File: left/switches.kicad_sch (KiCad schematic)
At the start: 38 parts, among them K11 KEYSW_RGB, K12 KEYSW_RGB, K13 KEYSW_RGB, K14 KEYSW_RGB, K15 KEYSW_RGB, K16 KEYSW_RGB, K21 KEYSW_RGB, K22 KEYSW_RGB, K23 KEYSW_RGB, K24 KEYSW_RGB, K25 KEYSW_RGB, K26 KEYSW_RGB, K31 KEYSW_RGB, K32 KEYSW_RGB, K33 KEYSW_RGB, K34 KEYSW_RGB, K35 KEYSW_RGB, K36 KEYSW_RGB, K41 KEYSW_RGB, K42 KEYSW_RGB, K43 KEYSW_RGB, K44 KEYSW_RGB, K45 KEYSW_RGB, K46 KEYSW_RGB, K51 KEYSW_RGB, K52 KEYSW_RGB, K53 KEYSW_RGB, K54 KEYSW_RGB, K55 KEYSW_RGB, K56 KEYSW_RGB, K61 KEYSW_RGB, K62 KEYSW_RGB, K63 KEYSW_RGB, K64 KEYSW_RGB, K65 KEYSW_RGB, K66 KEYSW_RGB, SW2 Rotary_Encoder_Switch

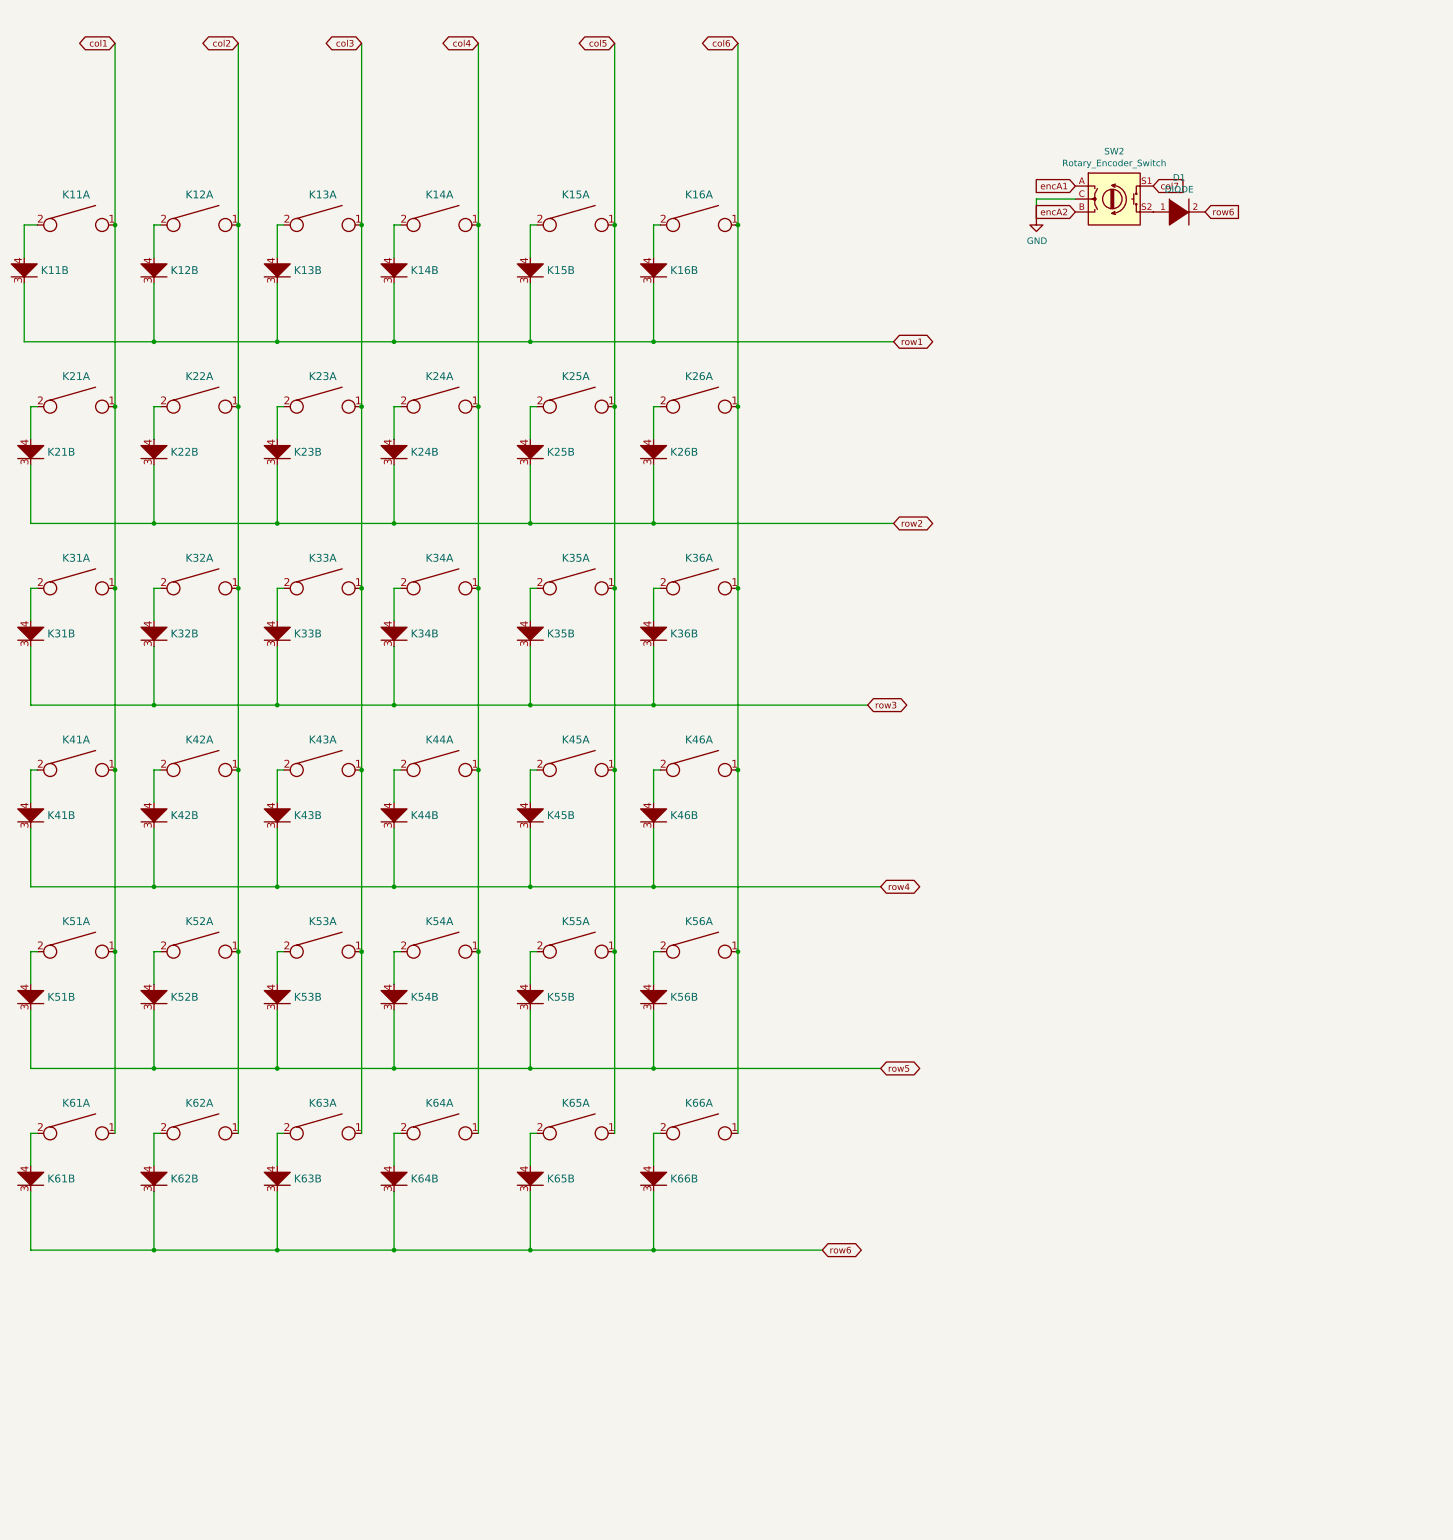
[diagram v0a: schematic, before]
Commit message: Broke out keys into individual components so that the BOM and pick and place are easier to generate.
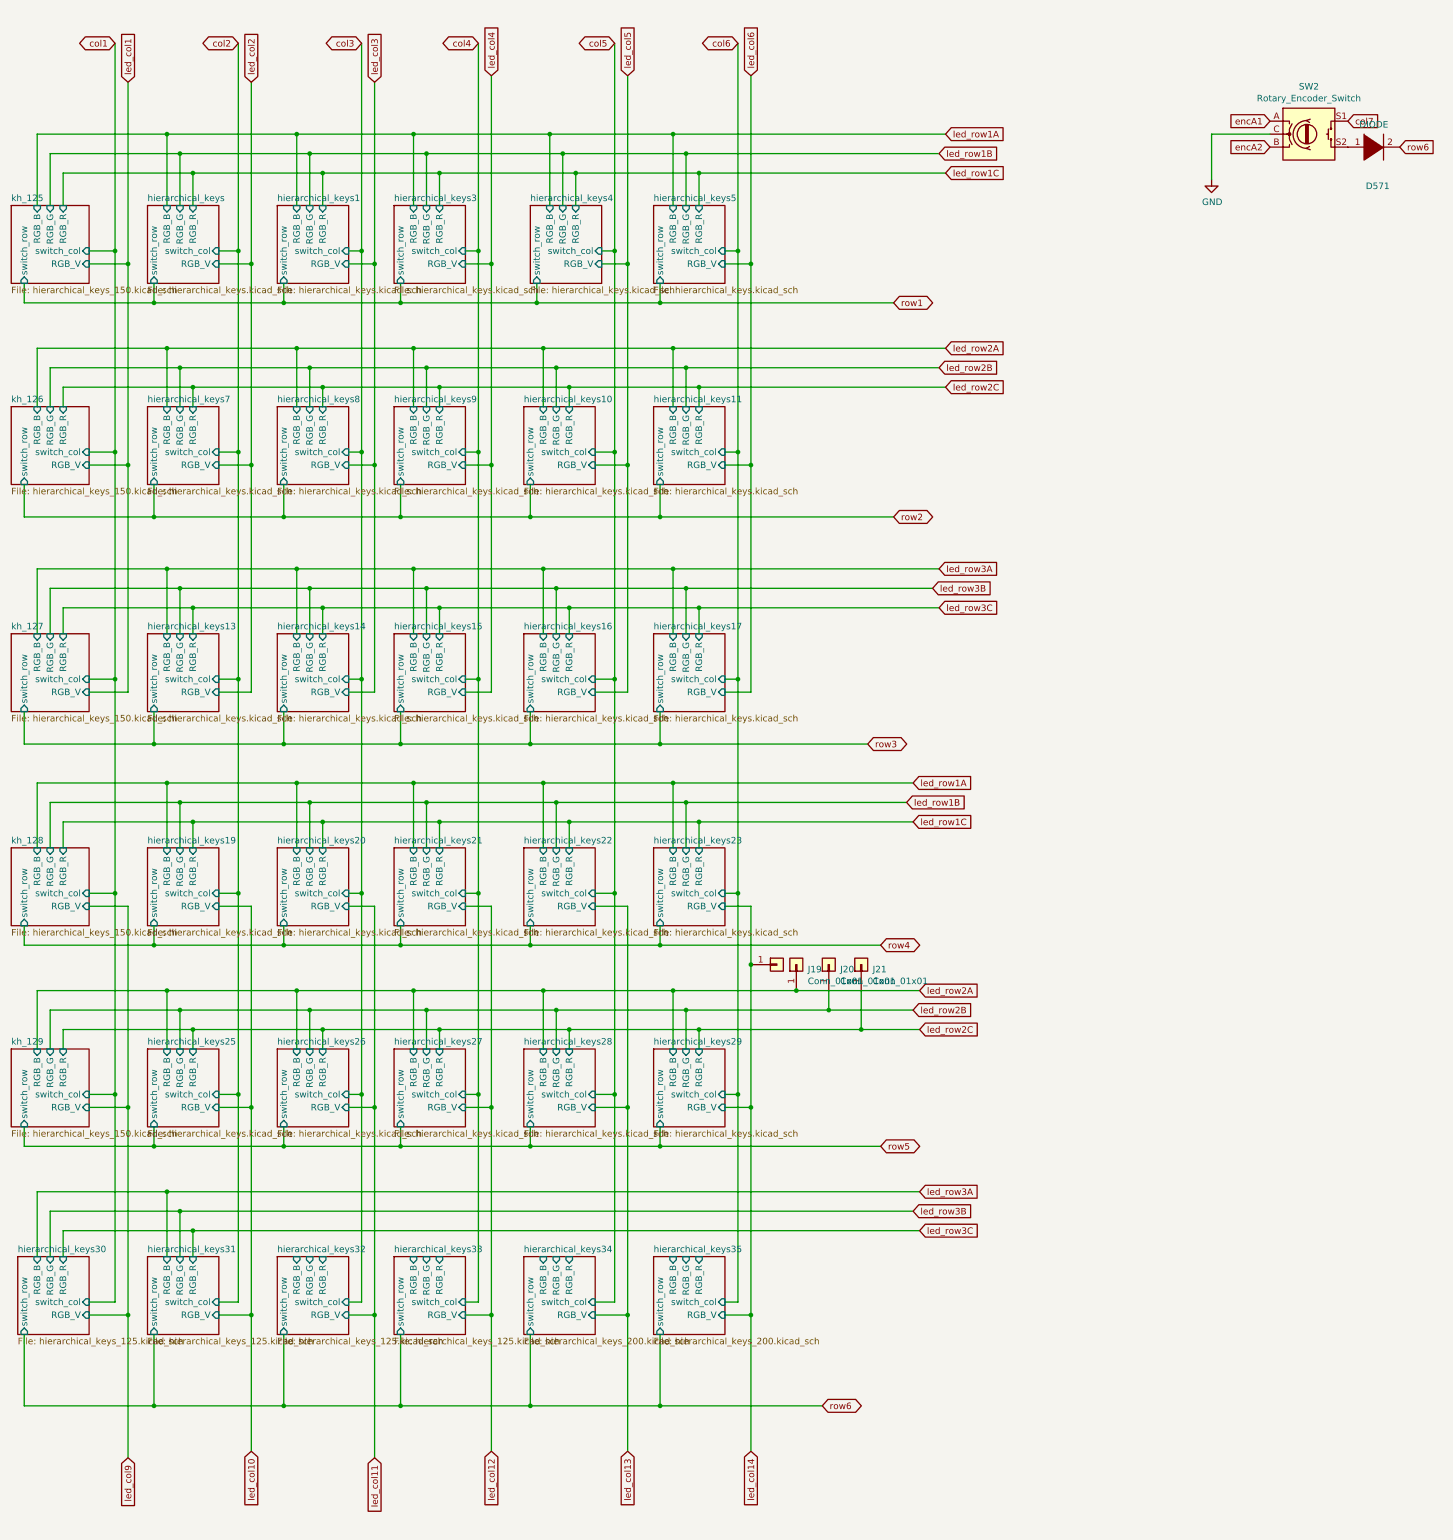
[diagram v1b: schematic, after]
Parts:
- removed K11, K21, K31, K41, K51: KEYSW_RGB, vladkvit_keyb:Hybrid_PCB_150H_hotswap_diode_RGB_rot, symbol vladkvit_keyb:KEYSW_RGB
- removed K12, K13, K14, K15, K16, K22, K23, K24, K25, K26, K32, K33, K34, K35, K36, K42, K43, K44, K45, K46, K52, K53, K54, K55, K56: KEYSW_RGB, vladkvit_keyb:Hybrid_PCB_100H_hotswap_diode_RGB_rot, symbol vladkvit_keyb:KEYSW_RGB
- removed K61, K62, K63, K64: KEYSW_RGB, vladkvit_keyb:Hybrid_PCB_125H_hotswap_diode_RGB_rot, symbol vladkvit_keyb:KEYSW_RGB
- removed K65, K66: KEYSW_RGB, vladkvit_keyb:Hybrid_PCB_200H_hotswap_diode_RGB, symbol vladkvit_keyb:KEYSW_RGB
- added J18, J19, J20, J21: Conn_01x01, TestPoint:TestPoint_Pad_D1.5mm, symbol Connector_Generic:Conn_01x01
- D571: renamed from D1; footprint Diode_SMD:D_0805_2012Metric_Pad1.15x1.40mm_HandSolder -> Diode_SMD:D_SOD-123
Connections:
- new net led_col14: J18.1 (Pin_1)
- new net led_row2A: J19.1 (Pin_1)
- new net led_row2B: J20.1 (Pin_1)
- new net led_row2C: J21.1 (Pin_1)
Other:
- added sheet hierarchical_keys (hierarchical_keys.kicad_sch)
- added sheet hierarchical_keys1 (hierarchical_keys.kicad_sch)
- added sheet hierarchical_keys10 (hierarchical_keys.kicad_sch)
- added sheet hierarchical_keys11 (hierarchical_keys.kicad_sch)
- added sheet hierarchical_keys13 (hierarchical_keys.kicad_sch)
- added sheet hierarchical_keys14 (hierarchical_keys.kicad_sch)
- added sheet hierarchical_keys15 (hierarchical_keys.kicad_sch)
- added sheet hierarchical_keys16 (hierarchical_keys.kicad_sch)
- added sheet hierarchical_keys17 (hierarchical_keys.kicad_sch)
- added sheet hierarchical_keys19 (hierarchical_keys.kicad_sch)
- added sheet hierarchical_keys20 (hierarchical_keys.kicad_sch)
- added sheet hierarchical_keys21 (hierarchical_keys.kicad_sch)
- added sheet hierarchical_keys22 (hierarchical_keys.kicad_sch)
- added sheet hierarchical_keys23 (hierarchical_keys.kicad_sch)
- added sheet hierarchical_keys25 (hierarchical_keys.kicad_sch)
- added sheet hierarchical_keys26 (hierarchical_keys.kicad_sch)
- added sheet hierarchical_keys27 (hierarchical_keys.kicad_sch)
- added sheet hierarchical_keys28 (hierarchical_keys.kicad_sch)
- added sheet hierarchical_keys29 (hierarchical_keys.kicad_sch)
- added sheet hierarchical_keys3 (hierarchical_keys.kicad_sch)
- added sheet hierarchical_keys30 (hierarchical_keys_125.kicad_sch)
- added sheet hierarchical_keys31 (hierarchical_keys_125.kicad_sch)
- added sheet hierarchical_keys32 (hierarchical_keys_125.kicad_sch)
- added sheet hierarchical_keys33 (hierarchical_keys_125.kicad_sch)
- added sheet hierarchical_keys34 (hierarchical_keys_200.kicad_sch)
- added sheet hierarchical_keys35 (hierarchical_keys_200.kicad_sch)
- added sheet hierarchical_keys4 (hierarchical_keys.kicad_sch)
- added sheet hierarchical_keys5 (hierarchical_keys.kicad_sch)
- added sheet hierarchical_keys7 (hierarchical_keys.kicad_sch)
- added sheet hierarchical_keys8 (hierarchical_keys.kicad_sch)
- added sheet hierarchical_keys9 (hierarchical_keys.kicad_sch)
- added sheet kh_125 (hierarchical_keys_150.kicad_sch)
- added sheet kh_126 (hierarchical_keys_150.kicad_sch)
- added sheet kh_127 (hierarchical_keys_150.kicad_sch)
- added sheet kh_128 (hierarchical_keys_150.kicad_sch)
- added sheet kh_129 (hierarchical_keys_150.kicad_sch)
- moved on the sheet: D571, SW2

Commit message: Kicad 9 upgrade.
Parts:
- D571: LCSC (none) -> C77978
- SW2: LCSC (none) -> C470742
